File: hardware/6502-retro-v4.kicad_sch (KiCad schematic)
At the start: 63 parts, among them J1 SDCARD, J10 USB-C Adapter, J11 EXP2, J2 SPI BUS, J3 GPIO, J4 CTS, J5 RTS, J6 UART, J7 JOY1, J8 SPK/AMP, J9 EXP1, U1 AT22V10, U10 6551, U11 AS6C4008, U12 74LS32, U13 VDP, U14 SN76489AN, U15 74LS244, U16 DS1813-5, U2 W65C22S, U3 W65C02S, U4 74HC138, U5 W65C22S, U6 27C512, U7 GAL16V8, U8 AS6C4008, U9 74HC273, Y1 4MHz, Y2 1.8432MHz

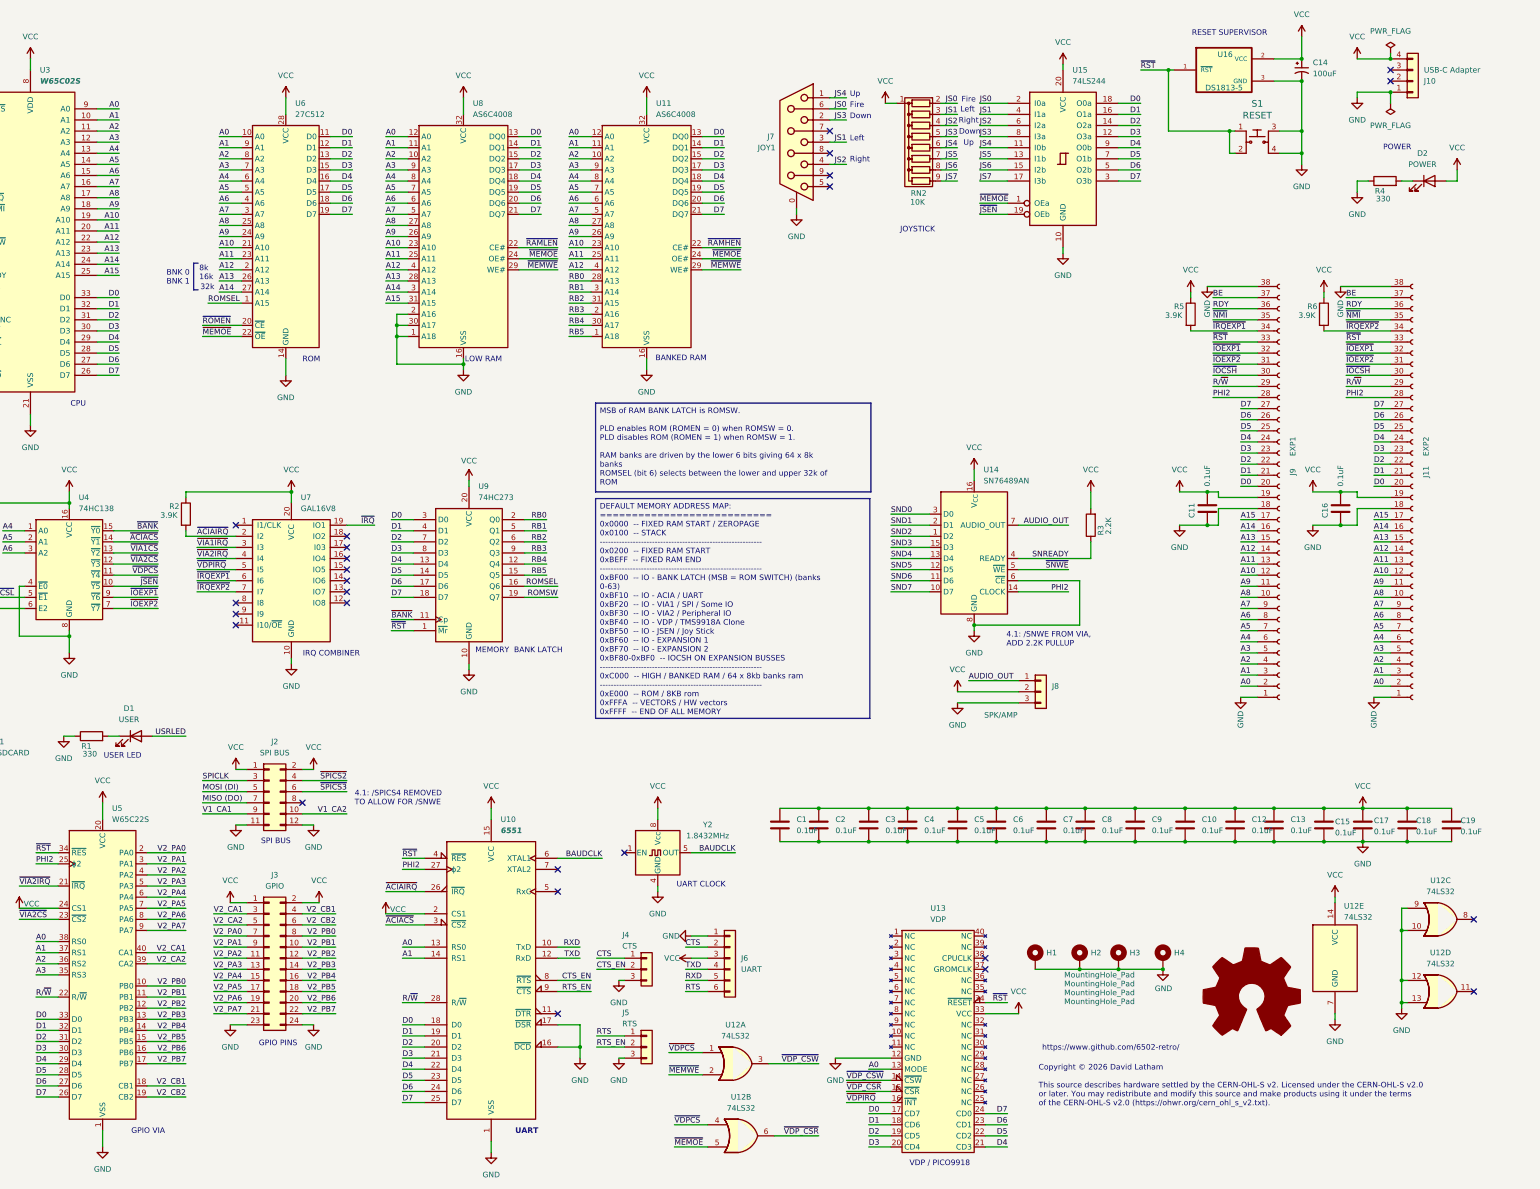
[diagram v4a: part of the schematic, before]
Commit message: Revisions to correct bugs found in v4.3
- Udd missing ground connections on Joystick port
- Correct enable pins on 74HCT244
- Relable support logic chips to HCT variants
- Re-route data pins on SN76489A PSG
- Change resistor value on power LED to 470ohm
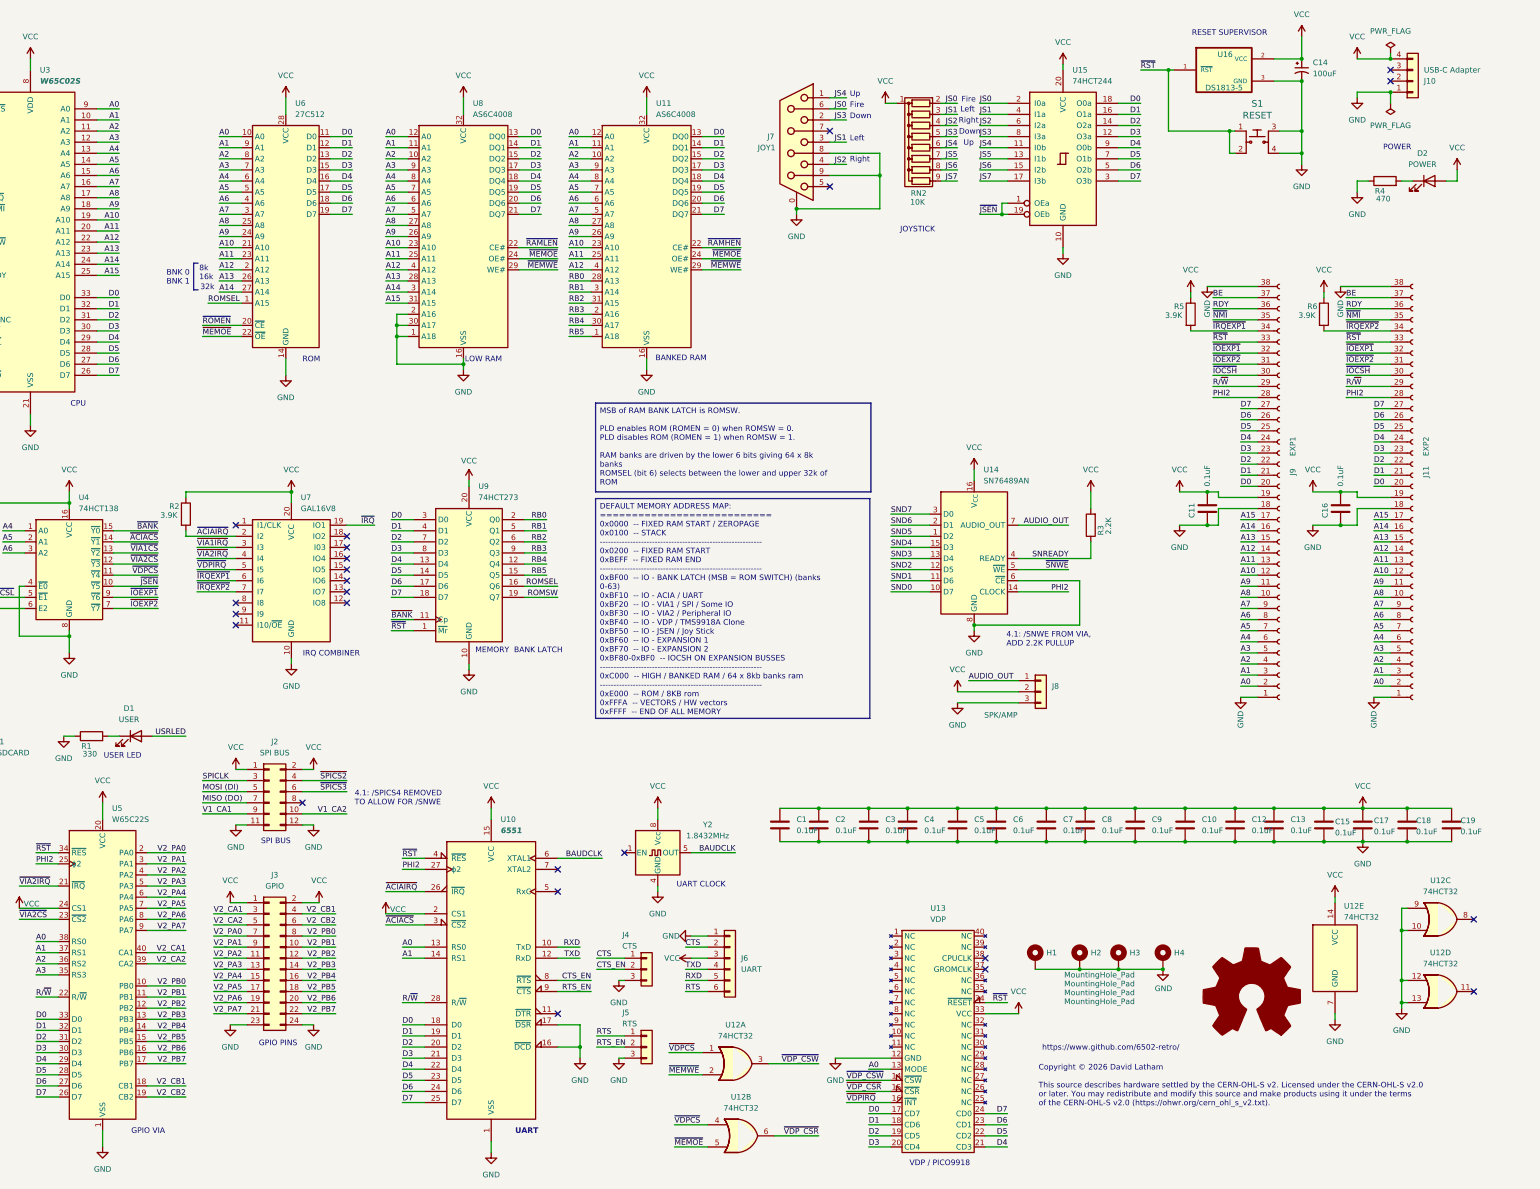
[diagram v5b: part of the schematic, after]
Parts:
- R4: value 330 -> 470
- U12: value 74LS32 -> 74HCT32
- U15: value 74LS244 -> 74HCT244
- U4: value 74HC138 -> 74HCT138
- U9: value 74HC273 -> 74HCT273
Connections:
- net GND: now also J7.8, J7.9
- net SND0: now also U14.10 (D7); no longer U14.3 (D0)
- net SND1: now also U14.11 (D6); no longer U14.2 (D1)
- net SND2: now also U14.12 (D5); no longer U14.1 (D2)
- net SND3: now also U14.13 (D4); no longer U14.15 (D3)
- net SND4: now also U14.15 (D3); no longer U14.13 (D4)
- net SND5: now also U14.1 (D2); no longer U14.12 (D5)
- net SND6: now also U14.2 (D1); no longer U14.11 (D6)
- net SND7: now also U14.3 (D0); no longer U14.10 (D7)
- net ~{JSEN}: now also U15.1 (OEa)
- net ~{MEMOE}: no longer U15.1 (OEa)
- no-connect marks 39 -> 37
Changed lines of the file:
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@@
 	(title_block
 		(title "6502-Retro!")
-		(date "2026-02-15")
-		(rev "4.3")
+		(date "2026-03-14")
+		(rev "4.4")
 	)
 	(text "Up"
@@
 	)
 	(junction
+		(at 246.38 59.69)
+		(diameter 0)
+		(color 0 0 0 0)
+	)
+	(junction
 		(at 375.92 204.47)
 		(diameter 0)
@@
 	)
 	(junction
+		(at 265.43 52.07)
+		(diameter 0)
+		(color 0 0 0 0)
+	)
+	(junction
 		(at 355.6 204.47)
 		(diameter 0)
@@
 	)
 	(junction
+		(at 293.37 60.96)
+		(diameter 0)
+		(color 0 0 0 0)
+	)
+	(junction
 		(at 384.81 224.79)
 		(diameter 0)
@@
 	)
 	(no_connect
-		(at 254 46.99)
-	)
-	(no_connect
 		(at 143.51 144.78)
 	)
@@
 	)
 	(no_connect
-		(at 254 52.07)
-	)
-	(no_connect
 		(at 118.11 154.94)
 	)
@@
 	(wire
 		(pts
-			(xy 267.97 142.24) (xy 276.86 142.24)
+			(xy 267.97 134.62) (xy 276.86 134.62)
 		)
 		(stroke
@@
 	(wire
 		(pts
+			(xy 254 46.99) (xy 265.43 46.99)
+		)
+		(stroke
+			(width 0)
+			(type default)
+		)
+	)
+	(wire
+		(pts
 			(xy 106.68 209.55) (xy 97.79 209.55)
 		)
@@
 	(wire
 		(pts
-			(xy 267.97 129.54) (xy 276.86 129.54)
+			(xy 267.97 147.32) (xy 276.86 147.32)
 		)
 		(stroke
@@
 	(wire
 		(pts
+			(xy 265.43 59.69) (xy 246.38 59.69)
+		)
+		(stroke
+			(width 0)
+			(type default)
+		)
+	)
+	(wire
+		(pts
 			(xy 57.15 143.51) (xy 48.26 143.51)
 		)
@@
 	(wire
 		(pts
+			(xy 254 52.07) (xy 265.43 52.07)
+		)
+		(stroke
+			(width 0)
+			(type default)
+		)
+	)
+	(wire
+		(pts
 			(xy 140.97 233.68) (xy 133.35 233.68)
 		)
@@
 	(wire
 		(pts
-			(xy 288.29 60.96) (xy 294.64 60.96)
+			(xy 288.29 60.96) (xy 293.37 60.96)
 		)
 		(stroke
@@
 	(wire
 		(pts
-			(xy 288.29 58.42) (xy 294.64 58.42)
-		)
-		(stroke
-			(width 0)
-			(type default)
-		)
-	)
-	(wire
-		(pts
 			(xy 80.01 124.46) (xy 80.01 127)
 		)
@@
 	(wire
 		(pts
-			(xy 267.97 139.7) (xy 276.86 139.7)
+			(xy 267.97 137.16) (xy 276.86 137.16)
 		)
 		(stroke
@@
 	(wire
 		(pts
-			(xy 267.97 132.08) (xy 276.86 132.08)
+			(xy 267.97 144.78) (xy 276.86 144.78)
 		)
 		(stroke
@@
 	(wire
 		(pts
-			(xy 267.97 137.16) (xy 276.86 137.16)
+			(xy 267.97 139.7) (xy 276.86 139.7)
 		)
 		(stroke
@@
 	(wire
 		(pts
-			(xy 267.97 144.78) (xy 276.86 144.78)
+			(xy 267.97 132.08) (xy 276.86 132.08)
 		)
 		(stroke
@@
 	(wire
 		(pts
-			(xy 267.97 147.32) (xy 276.86 147.32)
+			(xy 267.97 129.54) (xy 276.86 129.54)
 		)
 		(stroke
@@
 	(wire
 		(pts
+			(xy 294.64 58.42) (xy 293.37 58.42)
+		)
+		(stroke
+			(width 0)
+			(type default)
+		)
+	)
+	(wire
+		(pts
 			(xy 257.81 36.83) (xy 254 36.83)
 		)
@@
 	(wire
 		(pts
+			(xy 293.37 58.42) (xy 293.37 60.96)
+		)
+		(stroke
+			(width 0)
+			(type default)
+		)
+	)
+	(wire
+		(pts
 			(xy 106.68 212.09) (xy 97.79 212.09)
 		)
@@
 	(wire
 		(pts
+			(xy 265.43 52.07) (xy 265.43 59.69)
+		)
+		(stroke
+			(width 0)
+			(type default)
+		)
+	)
+	(wire
+		(pts
 			(xy 114.3 50.8) (xy 119.38 50.8)
 		)
@@
 	(wire
 		(pts
+			(xy 265.43 46.99) (xy 265.43 52.07)
+		)
+		(stroke
+			(width 0)
+			(type default)
+		)
+	)
+	(wire
+		(pts
 			(xy 58.42 232.41) (xy 48.26 232.41)
 		)
@@
 	(wire
 		(pts
+			(xy 293.37 60.96) (xy 294.64 60.96)
+		)
+		(stroke
+			(width 0)
+			(type default)
+		)
+	)
+	(wire
+		(pts
 			(xy 100.33 146.05) (xy 90.17 146.05)
 		)
@@
 	(wire
 		(pts
-			(xy 267.97 134.62) (xy 276.86 134.62)
+			(xy 267.97 142.24) (xy 276.86 142.24)
 		)
 		(stroke
@@
 	)
 	(label "SND7"
-		(at 267.97 147.32 0)
+		(at 267.97 129.54 0)
 		(effects
 			(font
@@
 	)
 	(label "SND5"
-		(at 267.97 142.24 0)
+		(at 267.97 134.62 0)
 		(effects
 			(font
@@
 		)
 	)
-	(label "~{MEMOE}"
-		(at 288.29 58.42 0)
-		(effects
-			(font
-				(size 1.27 1.27)
-			)
-			(justify left bottom)
-		)
-	)
 	(label "V2_PB1"
 		(at 106.68 240.03 180)
@@
 	)
 	(label "SND2"
-		(at 267.97 134.62 0)
+		(at 267.97 142.24 0)
 		(effects
 			(font
@@
 	)
 	(label "SND1"
-		(at 267.97 132.08 0)
+		(at 267.97 144.78 0)
 		(effects
 			(font
@@
 	)
 	(label "SND3"
-		(at 267.97 137.16 0)
+		(at 267.97 139.7 0)
 		(effects
 			(font
@@
 	)
 	(label "SND0"
-		(at 267.97 129.54 0)
+		(at 267.97 147.32 0)
 		(effects
 			(font
@@
 	)
 	(label "SND6"
-		(at 267.97 144.78 0)
+		(at 267.97 132.08 0)
 		(effects
 			(font
@@
 	)
 	(label "SND4"
-		(at 267.97 139.7 0)
+		(at 267.97 137.16 0)
 		(effects
 			(font
@@
 			)
 		)
-		(property "Value" "74HC138"
+		(property "Value" "74HCT138"
 			(at 82.1533 128.27 0)
 			(effects
@@
 			)
 		)
-		(property "Value" "74LS32"
+		(property "Value" "74HCT32"
 			(at 233.68 265.43 0)
 			(effects
@@
 			)
 		)
-		(property "Value" "74LS32"
+		(property "Value" "74HCT32"
 			(at 393.7 232.41 0)
 			(effects
@@
 			)
 		)
-		(property "Value" "74LS32"
+		(property "Value" "74HCT32"
 			(at 393.7 215.9 0)
 			(effects
@@
 			)
 		)
-		(property "Value" "330"
+		(property "Value" "470"
 			(at 382.27 57.404 90)
 			(effects
@@
 			)
 		)
-		(property "Value" "74LS32"
+		(property "Value" "74HCT32"
 			(at 232.41 248.92 0)
 			(effects
@@
 			)
 		)
-		(property "Value" "74LS244"
+		(property "Value" "74HCT244"
 			(at 309.4833 30.48 0)
 			(effects
@@
 			)
 		)
-		(property "Value" "74HC273"
+		(property "Value" "74HCT273"
 			(at 173.5933 125.73 0)
 			(effects
@@
 			)
 		)
-		(property "Value" "74LS32"
+		(property "Value" "74HCT32"
 			(at 371.602 221.742 0)
 			(effects
